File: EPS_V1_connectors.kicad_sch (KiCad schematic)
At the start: 14 parts, among them J1 Conn_01x18, J2 Conn_01x25, J3 Conn_01x9, J4 Conn_01x02, SW1 SWITCH, SW2 SWITCH, SW3 SWITCH

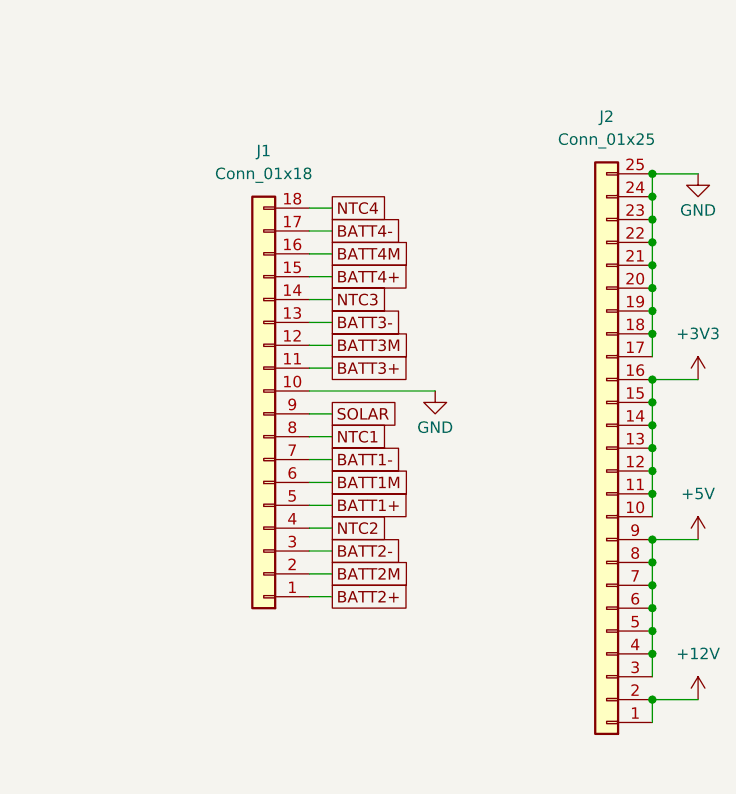
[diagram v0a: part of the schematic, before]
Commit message: Add CHG_OUT for heaters
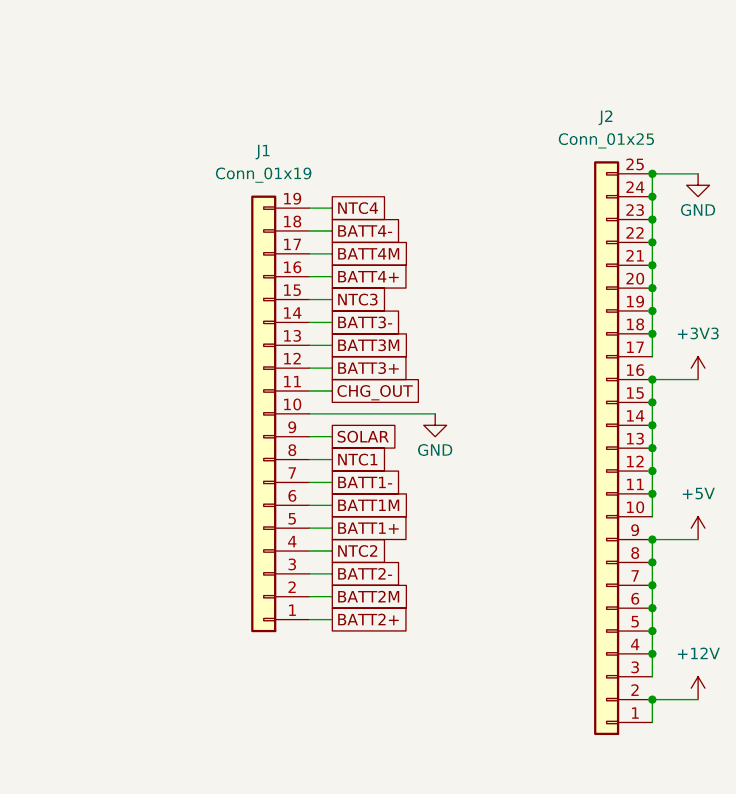
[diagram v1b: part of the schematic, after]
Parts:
- J1: value Conn_01x18 -> Conn_01x19; footprint Connector_PinHeader_2.54mm:PinHeader_1x18_P2.54mm_Vertical -> Connector_PinHeader_2.54mm:PinHeader_1x19_P2.54mm_Vertical; symbol Connector_Generic:Conn_01x18 -> Connector_Generic:Conn_01x19
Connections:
- net BATT3+: now also J1.12 (Pin_12); no longer J1.11 (Pin_11)
- net BATT3-: now also J1.14 (Pin_14); no longer J1.13 (Pin_13)
- net BATT3M: now also J1.13 (Pin_13); no longer J1.12 (Pin_12)
- net BATT4+: now also J1.16 (Pin_16); no longer J1.15 (Pin_15)
- net BATT4-: now also J1.18 (Pin_18); no longer J1.17 (Pin_17)
- net BATT4M: now also J1.17 (Pin_17); no longer J1.16 (Pin_16)
- net CHG_OUT: now also J1.11 (Pin_11)
- net NTC3: now also J1.15 (Pin_15); no longer J1.14 (Pin_14)
- net NTC4: now also J1.19 (Pin_19); no longer J1.18 (Pin_18)

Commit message: Relink footprint references to consolidated libs/footprints.pretty
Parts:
- NT10: footprint switches:RBF -> footprints:RBF
- SW1, SW3: footprint switches:SWITCH-R -> footprints:SWITCH-R
- SW2: footprint switches:SWITCH-L -> footprints:SWITCH-L
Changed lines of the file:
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@@
 			)
 		)
-		(property "Footprint" "switches:SWITCH-R"
+		(property "Footprint" "footprints:SWITCH-R"
 			(at 78.74 182.88 0)
 			(hide yes)
@@
 			)
 		)
-		(property "Footprint" "switches:SWITCH-R"
+		(property "Footprint" "footprints:SWITCH-R"
 			(at 238.76 86.36 0)
 			(hide yes)
@@
 			)
 		)
-		(property "Footprint" "switches:SWITCH-L"
+		(property "Footprint" "footprints:SWITCH-L"
 			(at 254 84.836 0)
 			(hide yes)
@@
 			)
 		)
-		(property "Footprint" "switches:RBF"
+		(property "Footprint" "footprints:RBF"
 			(at 219.71 80.01 0)
 			(hide yes)
